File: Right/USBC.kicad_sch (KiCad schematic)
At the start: 5 parts, among them J1 USB-C USB 2.0 MC-372, U28 USBLC6-2SC6

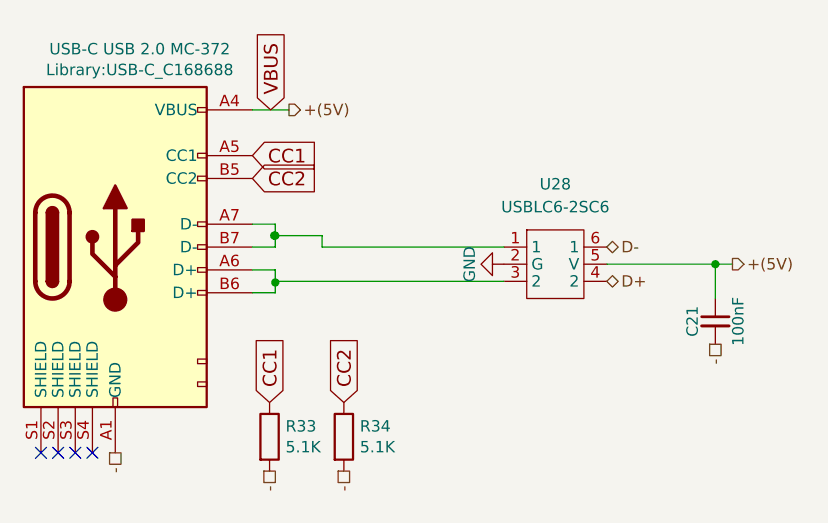
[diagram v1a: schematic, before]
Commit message: upgraded files to kicad7
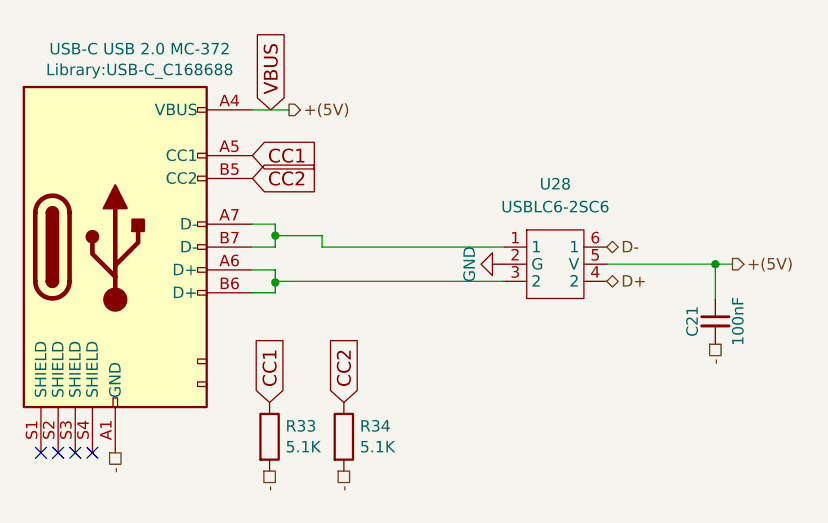
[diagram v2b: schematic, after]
